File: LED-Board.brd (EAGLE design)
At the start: 71 x 34 mm, 34 parts, among them U1 ATSAMD11C14A-SSUT, U3 LDL1117S12R

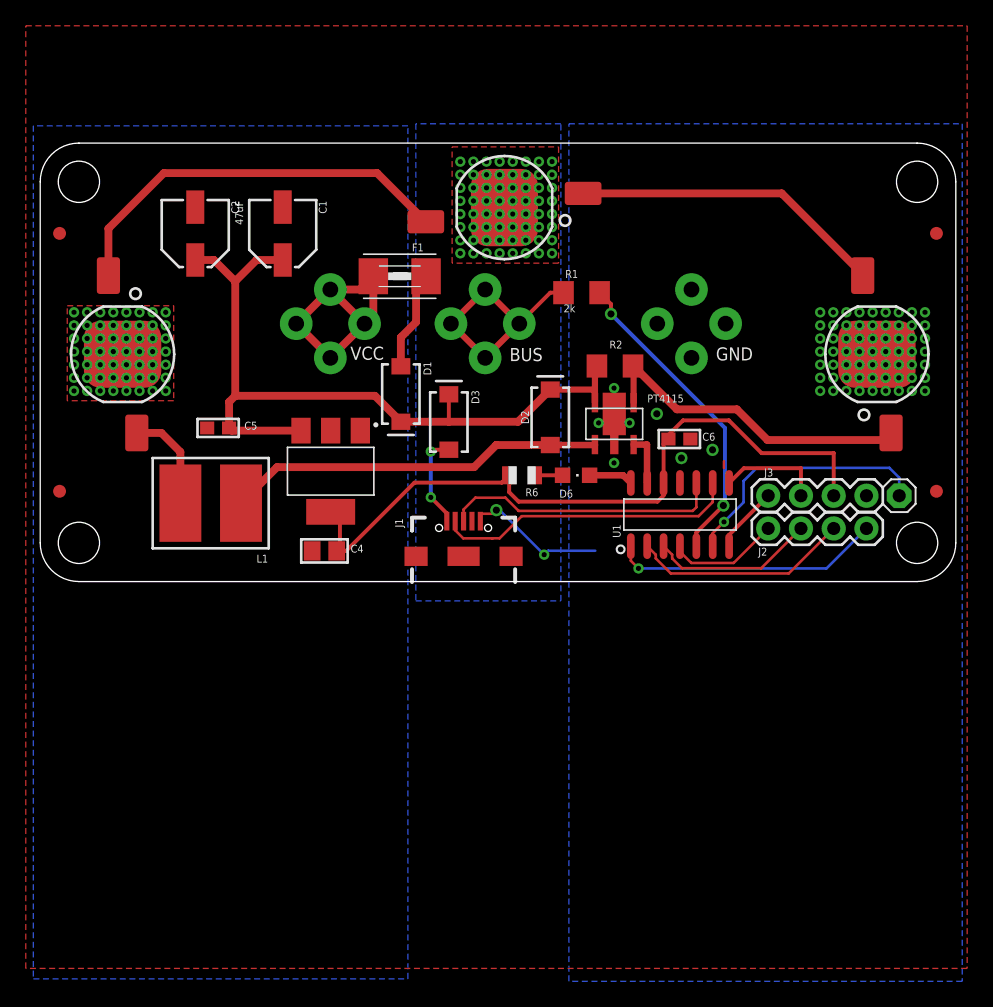
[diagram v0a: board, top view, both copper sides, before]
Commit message: added values/aligned names and values
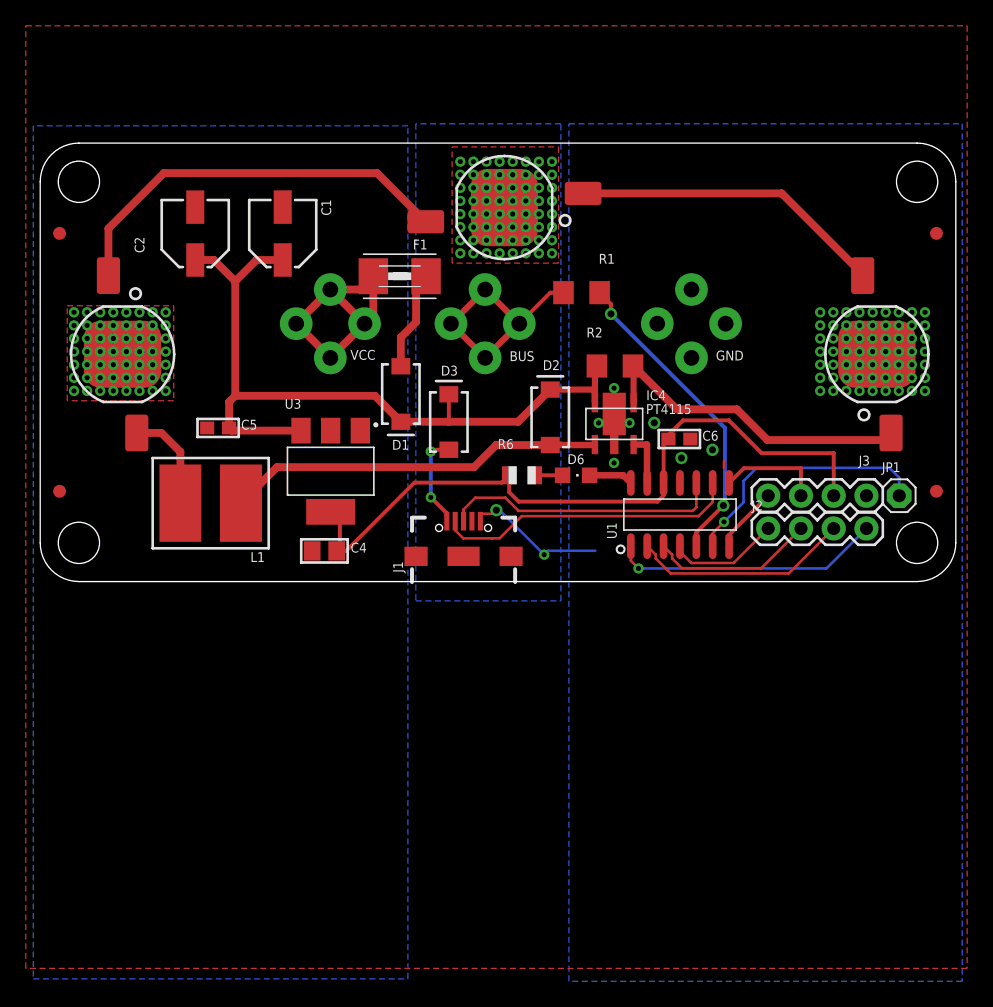
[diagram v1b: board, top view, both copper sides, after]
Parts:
- C2: value 100uF -> 100uF2
- R6: value (none) -> 59R

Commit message: exchanged j3 and c1/2 footprint of led module
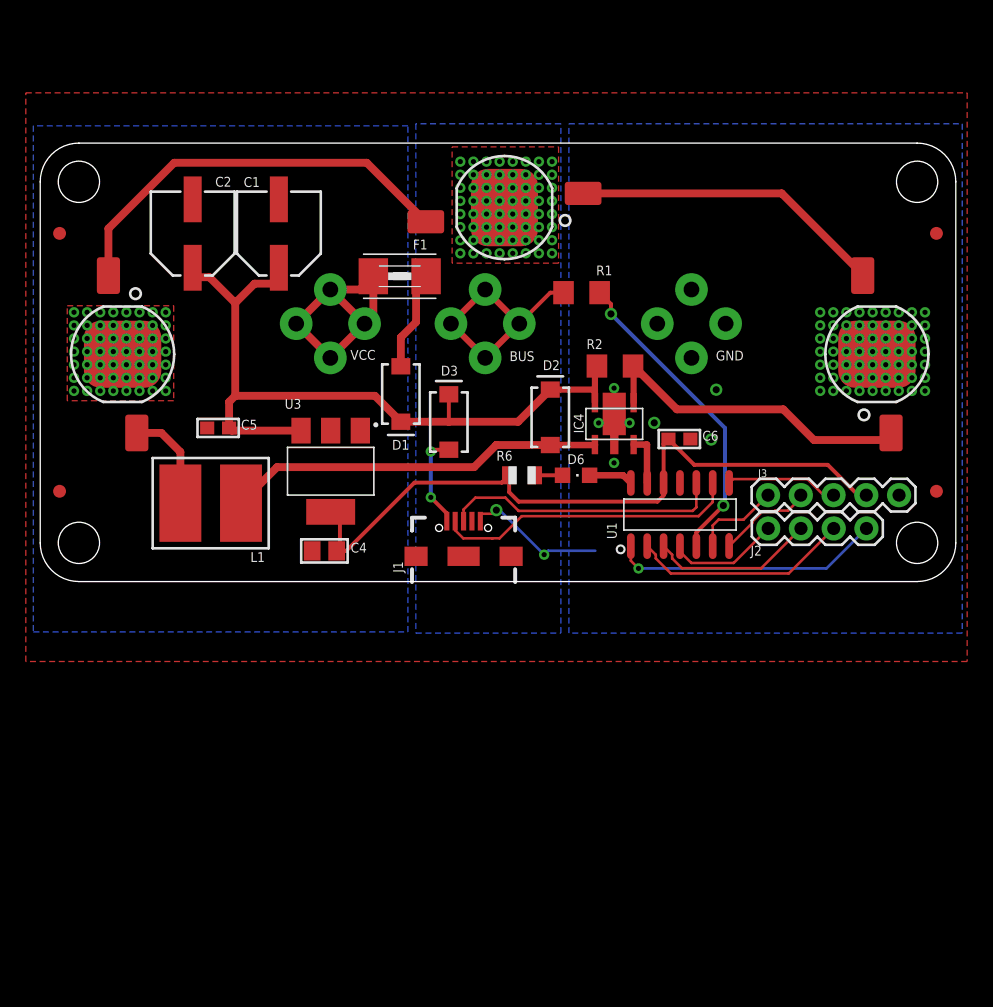
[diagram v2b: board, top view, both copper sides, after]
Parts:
- removed JP1: (no value), Adafruit:1X01
- C1: device microbuilder:PANASONIC_C -> microbuilder:PANASONIC_D
- C2: value 100uF2 -> 100uF; device microbuilder:PANASONIC_C -> microbuilder:PANASONIC_D
- J3: device SparkFun-Connectors:1X04 -> SparkFun-Connectors:1X05
- moved J3 2.53 mm to (66.6, 6.70)
- moved C1 0.30 mm to (18.5, 27.0)
- moved C2 0.20 mm to (11.8, 27.0)
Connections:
- removed net N$13: JP1.1, U1.6
- new net RESET: J3.5, U1.6
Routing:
- net N$13: track 20.2 -> 0.00 mm, vias 1 -> 0
- net RESET: track 0.00 -> 6.87 mm
- net SWCLK: track 5.17 -> 8.26 mm
- net VCC: track 61.3 -> 58.8 mm
- net N$3: track 31.6 -> 32.3 mm
- net SWDIO: track 8.18 -> 8.74 mm
- net GND: track 11.6 -> 11.1 mm
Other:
- board text removed: "PT4115"

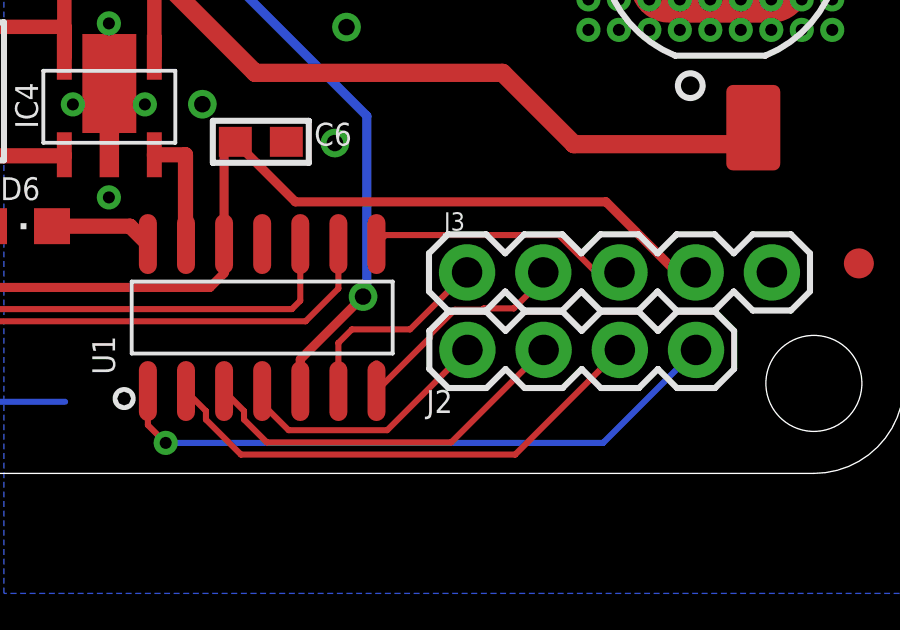
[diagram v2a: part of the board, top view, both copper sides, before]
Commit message: renamed some connectors
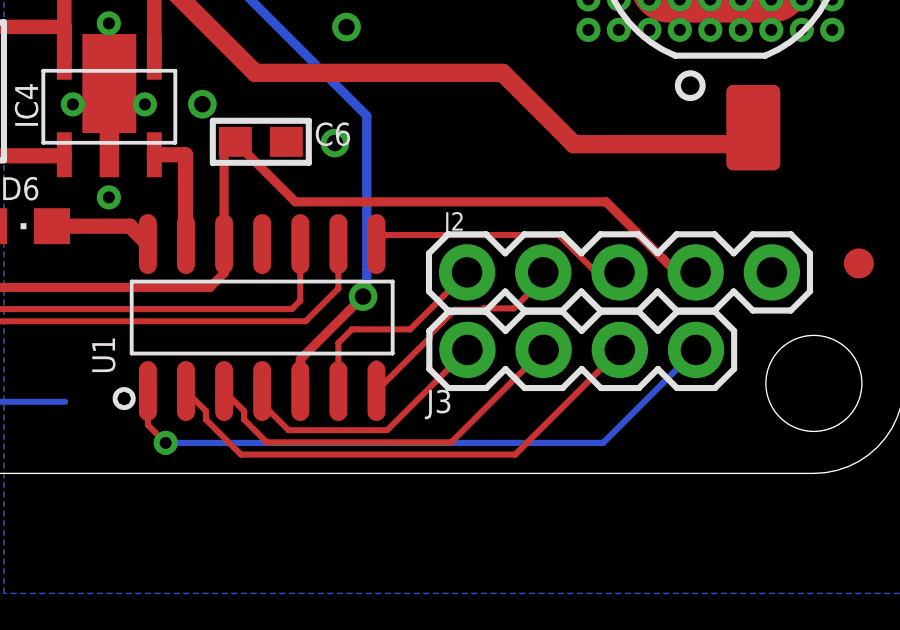
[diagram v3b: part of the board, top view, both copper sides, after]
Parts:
- J2: device SparkFun-Connectors:1X04 -> SparkFun-Connectors:1X05
- J3: device SparkFun-Connectors:1X05 -> SparkFun-Connectors:1X04
- moved J2 10.5 mm to (66.6, 6.70), turned to 180 degrees
- moved J3 10.5 mm to (56.5, 4.12), turned to 0 degrees
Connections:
- net 3.3V: now also J2.2; no longer J3.2
- net GND: now also J2.1; no longer J3.1
- net N$10: now also J3.4; no longer J2.4
- net N$7: now also J3.1; no longer J2.1
- net N$8: now also J3.2; no longer J2.2
- net N$9: now also J3.3; no longer J2.3
- net RESET: now also J2.5; no longer J3.5
- net SWCLK: now also J2.4; no longer J3.4
- net SWDIO: now also J2.3; no longer J3.3
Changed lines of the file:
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@@
 <attribute name="PROD_ID" value="DIO-09886" x="31.687" y="12.371" size="1.778" layer="27" rot="R90" display="off"/>
 </element>
-<element name="J2" library="SparkFun-Connectors" library_urn="urn:adsk.eagle:library:513" package="1X04" package3d_urn="urn:adsk.eagle:package:38085/1" value="" x="56.452" y="4.116" smashed="yes">
+<element name="J3" library="SparkFun-Connectors" library_urn="urn:adsk.eagle:library:513" package="1X04" package3d_urn="urn:adsk.eagle:package:38085/1" value="" x="56.452" y="4.116" smashed="yes">
 <attribute name="NAME" x="55.082" y="2.013" size="0.762" layer="25" font="vector" ratio="15"/>
 <attribute name="PROD_ID" value="CONN-09696" x="56.452" y="4.116" size="1.778" layer="27" display="off"/>
@@
 <element name="FD3" library="SparkFun-Aesthetics" package="FIDUCIAL-1X2" value="FIDUCIAL1X2" x="69.5" y="27" smashed="yes"/>
 <element name="FD4" library="SparkFun-Aesthetics" package="FIDUCIAL-1X2" value="FIDUCIAL1X2" x="69.5" y="7" smashed="yes"/>
-<element name="J3" library="SparkFun-Connectors" package="1X05" value="" x="66.6" y="6.7" smashed="yes" rot="R180">
+<element name="J2" library="SparkFun-Connectors" package="1X05" value="" x="66.6" y="6.7" smashed="yes" rot="R180">
 <attribute name="NAME" x="56.37" y="8.703" size="0.6096" layer="25" font="vector" ratio="20" rot="R180"/>
 <attribute name="VALUE" x="67.87" y="8.732" size="0.6096" layer="27" font="vector" ratio="20" rot="R180"/>
@@
 <via x="44.5" y="15" extent="1-16" drill="0.4"/>
 <via x="44.5" y="9.2" extent="1-16" drill="0.4"/>
-<contactref element="J3" pad="1"/>
+<contactref element="J2" pad="1"/>
 <wire x1="67.596" y1="20.88" x2="68.612" y2="20.88" width="0" layer="19" extent="1-1"/>
 <wire x1="66.58" y1="20.88" x2="67.596" y2="20.88" width="0" layer="19" extent="1-1"/>
@@
 <wire x1="48.34" y1="6.672" x2="48.34" y2="7.6452" width="0.3048" layer="1"/>
 <wire x1="36.3636" y1="6.9324" x2="37.0972" y2="6.1988" width="0.3048" layer="1"/>
-<contactref element="J3" pad="2"/>
+<contactref element="J2" pad="2"/>
 <wire x1="48.7156" y1="11.0532" x2="50.7172" y2="9.0516" width="0.3048" layer="1"/>
 <wire x1="63.42381875" y1="6.7" x2="64.06" y2="6.7" width="0.3048" layer="1"/>
@@
 <signal name="SWDIO">
 <contactref element="U1" pad="8"/>
-<contactref element="J3" pad="3"/>
+<contactref element="J2" pad="3"/>
 <wire x1="60.74013125" y1="6.7" x2="61.52" y2="6.7" width="0.2032" layer="1"/>
 <wire x1="59.49553125" y1="7.9446" x2="60.74013125" y2="6.7" width="0.2032" layer="1"/>
@@
 <contactref element="U1" pad="7"/>
 <wire x1="53.42" y1="2.7452" x2="53.42" y2="3.6188" width="0.3048" layer="1"/>
-<contactref element="J3" pad="4"/>
+<contactref element="J2" pad="4"/>
 <wire x1="53.42" y1="2.7452" x2="55.2074" y2="4.5326" width="0.2032" layer="1"/>
 <wire x1="55.2074" y1="4.5326" x2="55.2074" y2="4.63153125" width="0.2032" layer="1"/>
@@
 <signal name="N$7">
 <contactref element="U1" pad="4"/>
-<contactref element="J2" pad="1"/>
+<contactref element="J3" pad="1"/>
 <wire x1="49.61" y1="2.7452" x2="49.61" y2="2.322" width="0.2032" layer="1"/>
 <wire x1="50.4916" y1="1.4404" x2="53.7764" y2="1.4404" width="0.2032" layer="1"/>
@@
 <signal name="N$8">
 <contactref element="U1" pad="3"/>
-<contactref element="J2" pad="2"/>
+<contactref element="J3" pad="2"/>
 <wire x1="48.34" y1="2.7452" x2="49.0052" y2="2.08" width="0.2032" layer="1"/>
 <wire x1="49.0052" y1="2.08" x2="49.0052" y2="1.79468125" width="0.2032" layer="1"/>
@@
 <signal name="N$9">
 <contactref element="U1" pad="2"/>
-<contactref element="J2" pad="3"/>
+<contactref element="J3" pad="3"/>
 <wire x1="47.07" y1="2.7452" x2="47.7352" y2="2.08" width="0.2032" layer="1"/>
 <wire x1="47.7352" y1="2.08" x2="47.7352" y2="1.79468125" width="0.2032" layer="1"/>
@@
 <signal name="N$10">
 <contactref element="U1" pad="1"/>
-<contactref element="J2" pad="4"/>
+<contactref element="J3" pad="4"/>
 <wire x1="45.8" y1="2.7452" x2="45.8" y2="1.6108" width="0.2032" layer="1"/>
 <wire x1="45.8" y1="1.6108" x2="46.3936" y2="1.0172" width="0.2032" layer="1"/>
@@
 <signal name="RESET">
 <contactref element="U1" pad="6"/>
-<contactref element="J3" pad="5"/>
+<contactref element="J2" pad="5"/>
 <wire x1="52.15" y1="2.7452" x2="52.15" y2="4.35" width="0.2032" layer="1"/>
 <wire x1="52.15" y1="4.35" x2="52.6" y2="4.8" width="0.2032" layer="1"/>

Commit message: added values
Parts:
- C5: value 1uF -> 10uF
- C6: value (none) -> 10uF
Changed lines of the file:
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@@
 <attribute name="VALUE" x="17.22" y="10.579" size="0.4064" layer="27" ratio="10" rot="R180"/>
 </element>
-<element name="C6" library="microbuilder" package="0603" value="" x="49.5656" y="11.0532" smashed="yes">
+<element name="C6" library="microbuilder" package="0603" value="10uF" x="49.5656" y="11.0532" smashed="yes">
 <attribute name="NAME" x="51.3436" y="10.9262" size="0.762" layer="25" font="vector" ratio="15"/>
 <attribute name="VALUE" x="51.3436" y="10.2912" size="0.4064" layer="27" font="vector" ratio="10"/>
@@
 <attribute name="VALUE" x="24.07" y="1.613" size="0.762" layer="27" font="vector" ratio="15"/>
 </element>
-<element name="C5" library="microbuilder" package="0603" value="1uF" x="13.797" y="11.91" smashed="yes">
+<element name="C5" library="microbuilder" package="0603" value="10uF" x="13.797" y="11.91" smashed="yes">
 <attribute name="NAME" x="15.575" y="11.783" size="0.762" layer="25" font="vector" ratio="15"/>
 <attribute name="VALUE" x="15.575" y="11.148" size="0.762" layer="27" font="vector" ratio="15"/>

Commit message: modified c6 to 1uF
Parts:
- C6: value 10uF -> 1uF
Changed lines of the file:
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@@
 <drawing>
 <settings>
-<setting alwaysvectorfont="yes"/>
+<setting alwaysvectorfont="no"/>
 <setting keepoldvectorfont="yes"/>
 <setting verticaltext="up"/>
@@
 <attribute name="VALUE" x="17.22" y="10.579" size="0.4064" layer="27" ratio="10" rot="R180"/>
 </element>
-<element name="C6" library="microbuilder" package="0603" value="10uF" x="49.5656" y="11.0532" smashed="yes">
+<element name="C6" library="microbuilder" package="0603" value="1uF" x="49.5656" y="11.0532" smashed="yes">
 <attribute name="NAME" x="51.3436" y="10.9262" size="0.762" layer="25" font="vector" ratio="15"/>
 <attribute name="VALUE" x="51.3436" y="10.2912" size="0.4064" layer="27" font="vector" ratio="10"/>
